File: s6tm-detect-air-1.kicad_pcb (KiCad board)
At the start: 2 copper layers, 67 x 67 mm, 81 parts, among them J1 Conn_01x04, J2 TC2030, J3 Conn_01x04, J4 Conn_01x04, J5 Conn_01x04_Pin, SW1 SW_Push, SW2 SW_Push, U1 SYS1002-H2, U10 004-1-0100, U2 MiCS-5524, U3 LMC6482, U4 HT753-1, U5 SN65HVD230, U6 STM32F103C8Tx, U7 HTU21, U8 LM73100, U9 ENS16x, Y1 8M

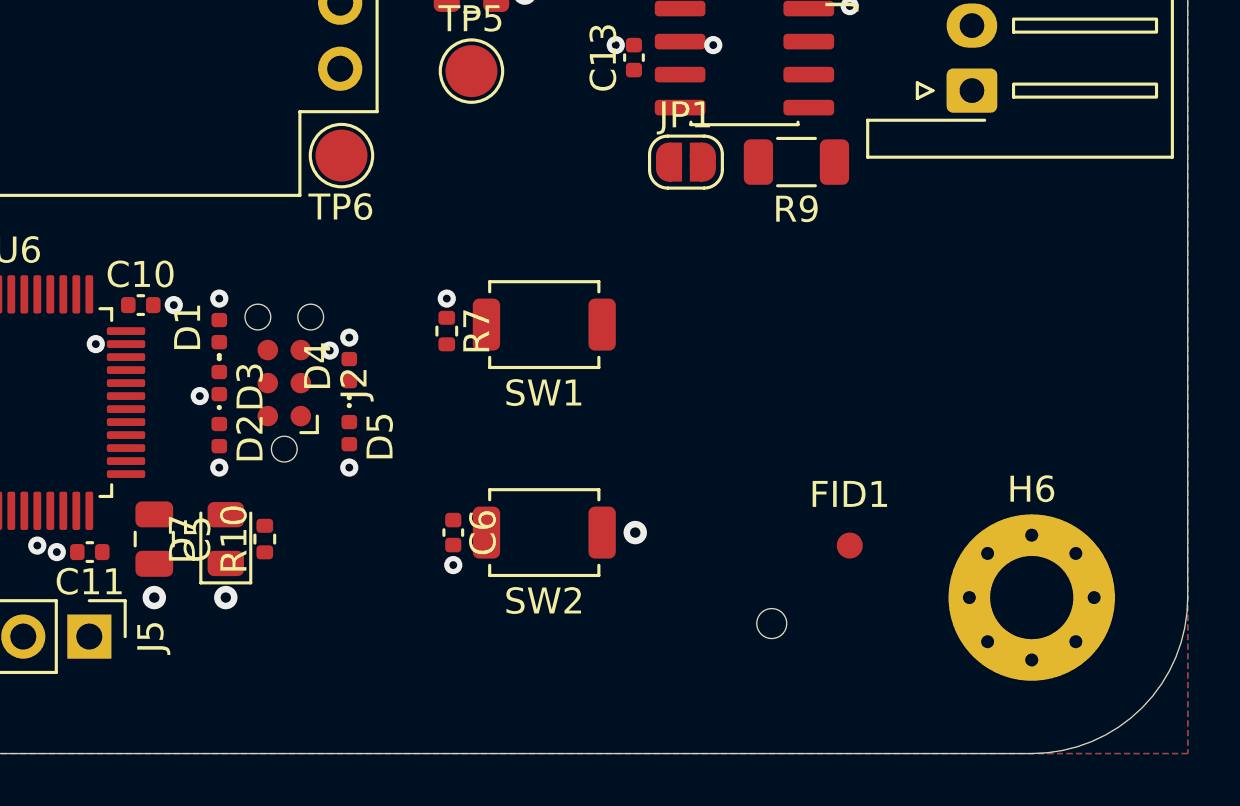
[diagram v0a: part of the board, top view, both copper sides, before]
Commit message: pcb/schem: add spare gpios header
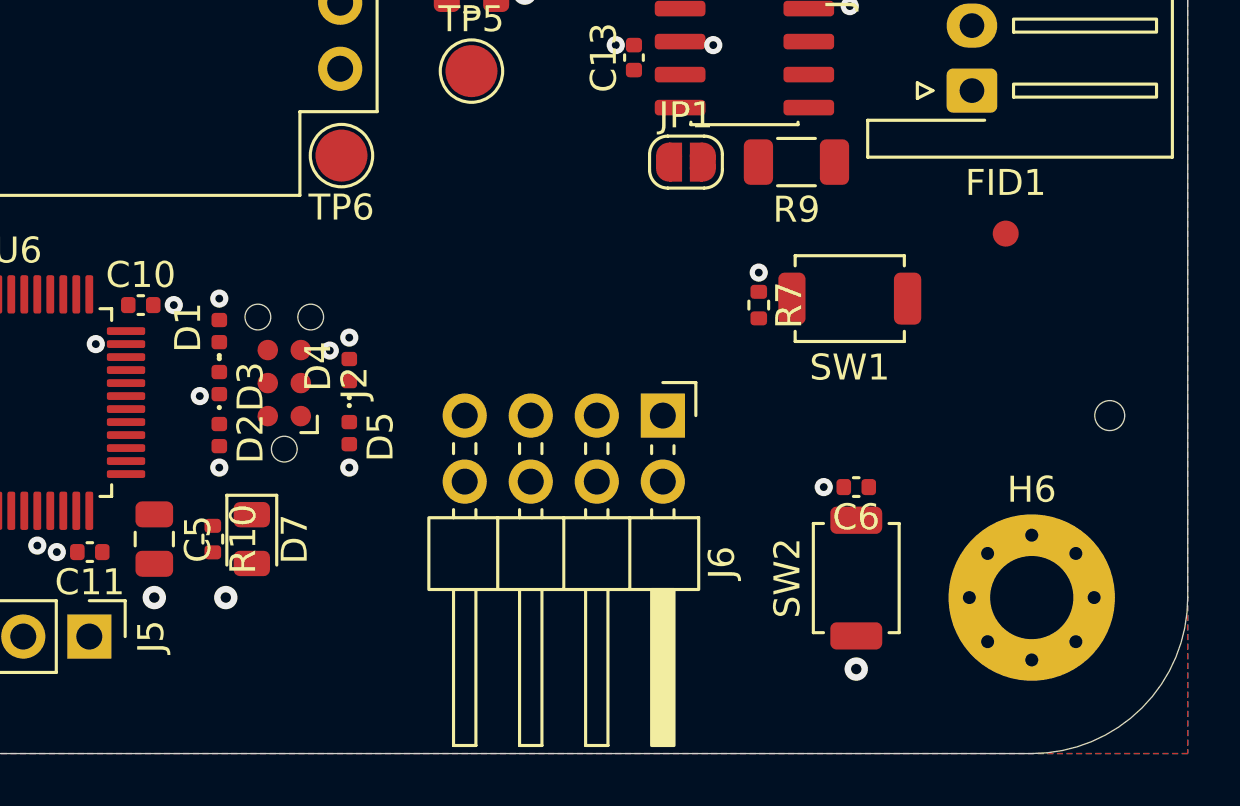
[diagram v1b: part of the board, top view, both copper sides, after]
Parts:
- added J6: Conn_01x08, Connector_PinHeader_2.54mm:PinHeader_2x04_P2.54mm_Horizontal, F.Cu at (161.8, 107.0)
- moved C6 15.6 mm to (169.2, 109.8), turned to 180 degrees
- moved H3 15.3 mm to (179.0, 107.0)
- moved FID1 13.4 mm to (175.0, 100.0)
- moved SW2 12.1 mm to (169.2, 113.2), turned to 90 degrees
- moved R7 12.0 mm to (165.5, 102.8)
- moved SW1 11.8 mm to (169.0, 102.5)
- moved R10 2.00 mm to (144.5, 111.8), turned to -90 degrees
- moved D7 1.00 mm to (146.0, 111.8), turned to -90 degrees
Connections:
- U6 pad 26: unconnected-(U6-PB13-Pad26) -> /PB13
- U6 pad 27: unconnected-(U6-PB14-Pad27) -> /PB14
- U6 pad 28: unconnected-(U6-PB15-Pad28) -> /PB15
- U6 pad 29: unconnected-(U6-PA8-Pad29) -> /PA8

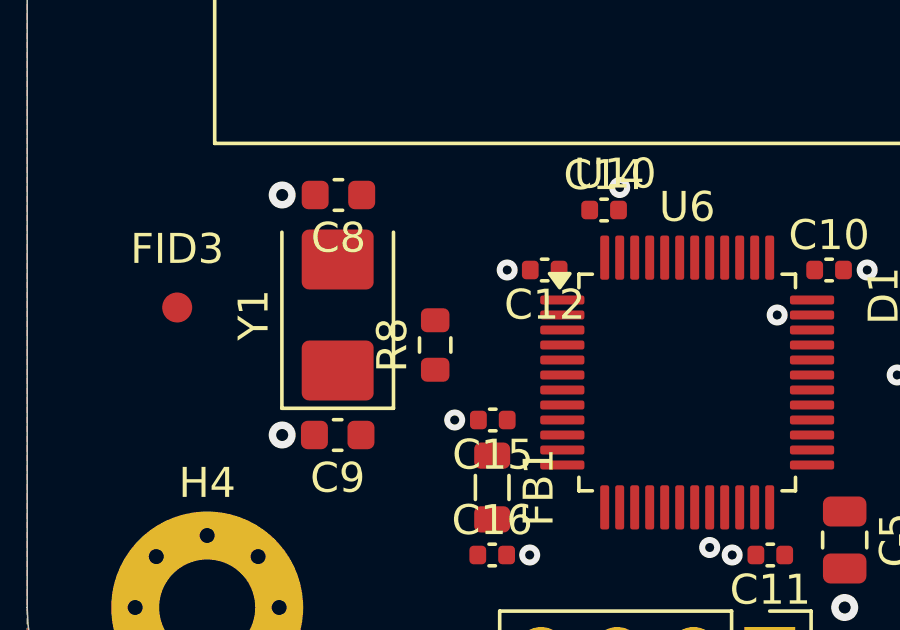
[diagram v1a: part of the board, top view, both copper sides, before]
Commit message: pcb: add crystal routing
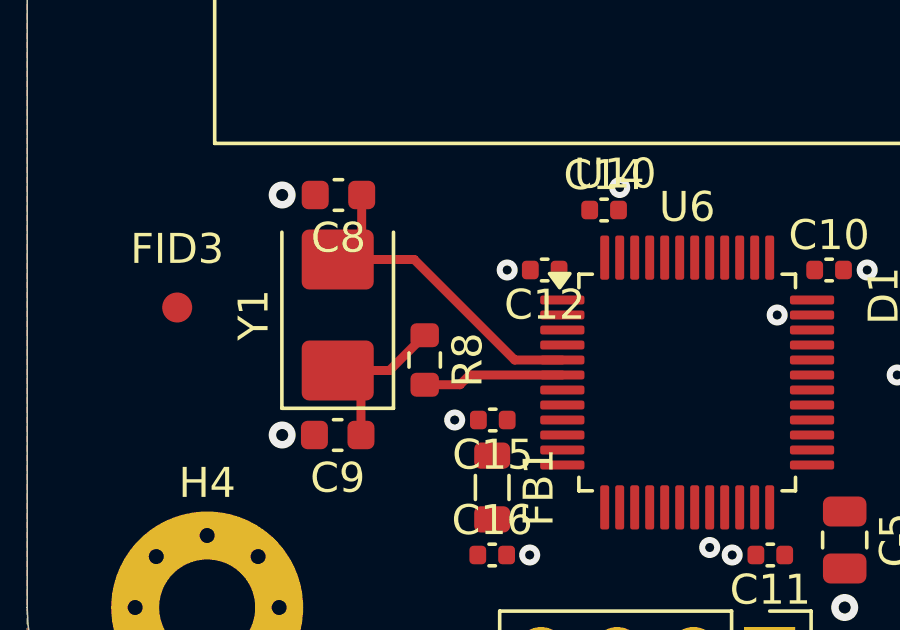
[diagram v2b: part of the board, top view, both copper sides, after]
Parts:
- moved R8 0.61 mm to (128.2, 105.8), turned to -90 degrees
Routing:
- net /XTAL_I: track 0.00 -> 11.4 mm
- net /XTAL_RO: track 0.00 -> 5.86 mm
- net /XTAL_O: track 0.00 -> 4.72 mm
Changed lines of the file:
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@@
 	(footprint "Resistor_SMD:R_0603_1608Metric"
 		(layer "F.Cu")
-		(at 128.6 105.25 90)
+		(at 128.25 105.75 -90)
 		(descr "Resistor SMD 0603 (1608 Metric), square (rectangular) end terminal, IPC-7351 nominal, (Body size source: IPC-SM-782 page 72, https://www.pcb-3d.com/wordpress/wp-content/uploads/ipc-sm-782a_amendment_1_and_2.pdf)")
 		(tags "resistor")
@@
 		)
 		(property "Basic" "Y"
-			(at 0 0 90)
+			(at 0 0 270)
 			(unlocked yes)
 			(layer "F.Fab")
@@
 		)
 		(property "JLCPCB Part #" "C23204"
-			(at 0 0 90)
+			(at 0 0 270)
 			(unlocked yes)
 			(layer "F.Fab")
@@
 		)
 		(property "Manufacturer" "Uniroyal Elec"
-			(at 0 0 90)
+			(at 0 0 270)
 			(unlocked yes)
 			(layer "F.Fab")
@@
 		)
 		(property "Manufacturer Part Number" "0603WAF5600T5E"
-			(at 0 0 90)
+			(at 0 0 270)
 			(unlocked yes)
 			(layer "F.Fab")
@@
 		(duplicate_pad_numbers_are_jumpers no)
 		(fp_line
-			(start -0.237258 -0.5225)
-			(end 0.237258 -0.5225)
+			(start -0.237258 0.5225)
+			(end 0.237258 0.5225)
 			(stroke
 				(width 0.12)
@@
 		)
 		(fp_line
-			(start -0.237258 0.5225)
-			(end 0.237258 0.5225)
+			(start -0.237258 -0.5225)
+			(end 0.237258 -0.5225)
 			(stroke
 				(width 0.12)
@@
 		)
 		(pad "1" smd roundrect
-			(at -0.825 0 90)
+			(at -0.825 0 270)
 			(size 0.8 0.95)
 			(layers "F.Cu" "F.Mask" "F.Paste")
@@
 		)
 		(pad "2" smd roundrect
-			(at 0.825 0 90)
+			(at 0.825 0 270)
 			(size 0.8 0.95)
 			(layers "F.Cu" "F.Mask" "F.Paste")
@@
 		(net "GND")
 	)
+	(segment
+		(start 127.9 102.4)
+		(end 131.25 105.75)
+		(width 0.3)
+		(layer "F.Cu")
+		(net "/XTAL_I")
+	)
+	(segment
+		(start 131.25 105.75)
+		(end 132.8375 105.75)
+		(width 0.3)
+		(layer "F.Cu")
+		(net "/XTAL_I")
+	)
+	(segment
+		(start 125.35 102.4)
+		(end 127.9 102.4)
+		(width 0.3)
+		(layer "F.Cu")
+		(net "/XTAL_I")
+	)
+	(segment
+		(start 126.15 101.6)
+		(end 125.35 102.4)
+		(width 0.3)
+		(layer "F.Cu")
+		(net "/XTAL_I")
+	)
+	(segment
+		(start 126.15 100.25)
+		(end 126.15 101.6)
+		(width 0.3)
+		(layer "F.Cu")
+		(net "/XTAL_I")
+	)
+	(segment
+		(start 128.25 104.925)
+		(end 127.075 106.1)
+		(width 0.3)
+		(layer "F.Cu")
+		(net "/XTAL_RO")
+	)
+	(segment
+		(start 126.125 106.875)
+		(end 125.35 106.1)
+		(width 0.3)
+		(layer "F.Cu")
+		(net "/XTAL_RO")
+	)
+	(segment
+		(start 127.075 106.1)
+		(end 125.35 106.1)
+		(width 0.3)
+		(layer "F.Cu")
+		(net "/XTAL_RO")
+	)
+	(segment
+		(start 126.125 108.25)
+		(end 126.125 106.875)
+		(width 0.3)
+		(layer "F.Cu")
+		(net "/XTAL_RO")
+	)
+	(segment
+		(start 129.75 106.25)
+		(end 129.425 106.575)
+		(width 0.3)
+		(layer "F.Cu")
+		(net "/XTAL_O")
+	)
+	(segment
+		(start 132.8375 106.25)
+		(end 129.75 106.25)
+		(width 0.3)
+		(layer "F.Cu")
+		(net "/XTAL_O")
+	)
+	(segment
+		(start 129.425 106.575)
+		(end 128.25 106.575)
+		(width 0.3)
+		(layer "F.Cu")
+		(net "/XTAL_O")
+	)
 	(zone

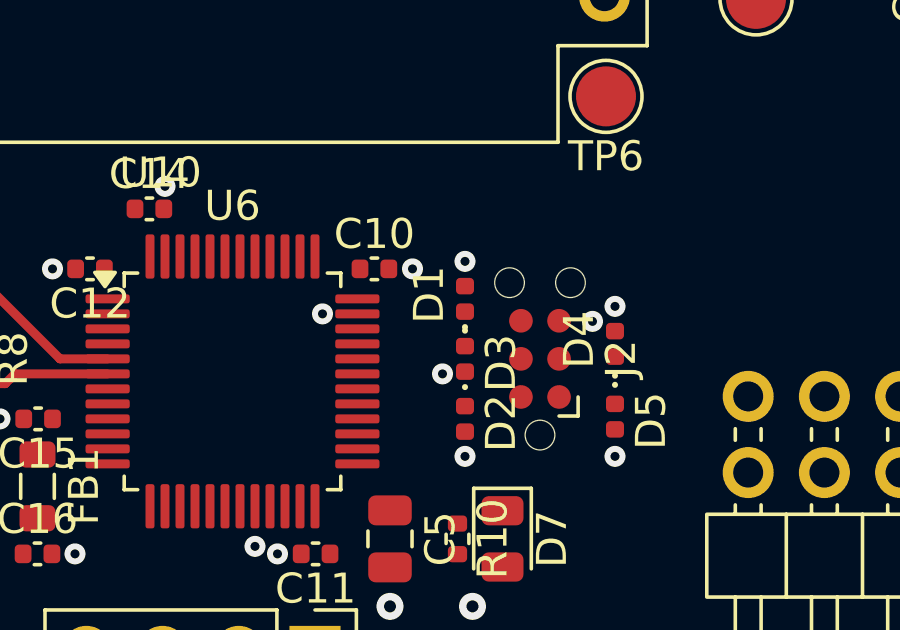
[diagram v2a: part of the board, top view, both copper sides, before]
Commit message: pcb: add swd routing
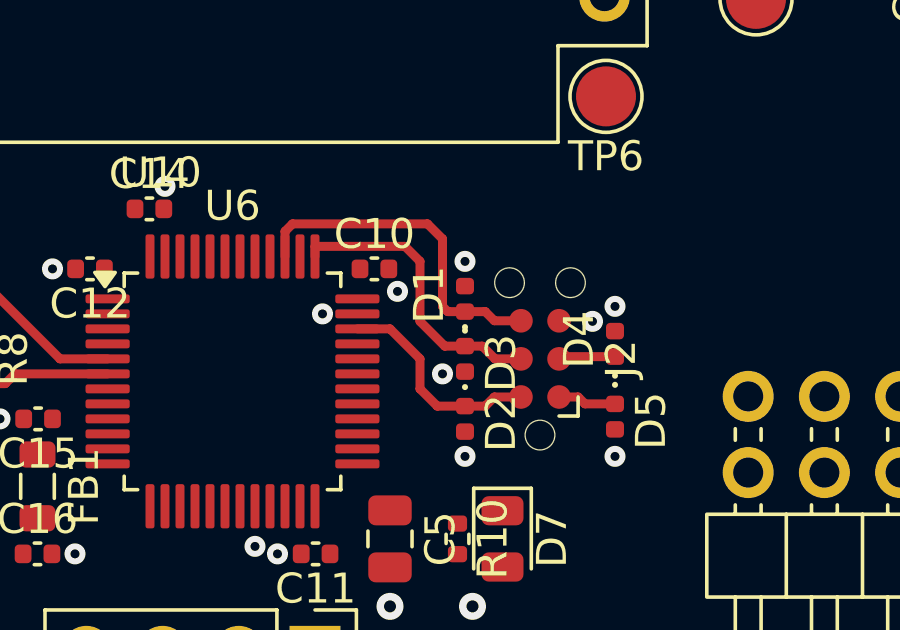
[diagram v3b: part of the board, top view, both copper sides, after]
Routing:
- net /SWO: track 0.00 -> 11.5 mm
- net /SWCLK: track 0.00 -> 9.93 mm
- net /SWDIO: track 0.00 -> 7.23 mm
- net +3V3: track 0.00 -> 1.96 mm
- net /NRST: track 0.00 -> 1.90 mm
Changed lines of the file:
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@@
 	)
 	(via
-		(at 143 102.75)
+		(at 142.5 103.5)
 		(size 0.7)
 		(drill 0.3)
@@
 		(free yes)
 		(net "GND")
+	)
+	(segment
+		(start 149.75 107.25)
+		(end 148.75 107.25)
+		(width 0.3)
+		(layer "F.Cu")
+		(net "+3V3")
+	)
+	(segment
+		(start 148.75 107.25)
+		(end 148.52 107.02)
+		(width 0.3)
+		(layer "F.Cu")
+		(net "+3V3")
+	)
+	(segment
+		(start 147.885 107.02)
+		(end 148.52 107.02)
+		(width 0.3)
+		(layer "F.Cu")
+		(net "+3V3")
 	)
 	(segment
@@
 	)
 	(segment
+		(start 139 101.25)
+		(end 138.75 101.5)
+		(width 0.3)
+		(layer "F.Cu")
+		(net "/SWO")
+	)
+	(segment
+		(start 144.75 104.175)
+		(end 144.175 104.175)
+		(width 0.3)
+		(layer "F.Cu")
+		(net "/SWO")
+	)
+	(segment
+		(start 144 101.75)
+		(end 143.5 101.25)
+		(width 0.3)
+		(layer "F.Cu")
+		(net "/SWO")
+	)
+	(segment
+		(start 143.5 101.25)
+		(end 139 101.25)
+		(width 0.3)
+		(layer "F.Cu")
+		(net "/SWO")
+	)
+	(segment
+		(start 144 104)
+		(end 144 101.75)
+		(width 0.3)
+		(layer "F.Cu")
+		(net "/SWO")
+	)
+	(segment
+		(start 144.75 104.175)
+		(end 145.425 104.175)
+		(width 0.3)
+		(layer "F.Cu")
+		(net "/SWO")
+	)
+	(segment
+		(start 145.73 104.48)
+		(end 146.615 104.48)
+		(width 0.3)
+		(layer "F.Cu")
+		(net "/SWO")
+	)
+	(segment
+		(start 144.175 104.175)
+		(end 144 104)
+		(width 0.3)
+		(layer "F.Cu")
+		(net "/SWO")
+	)
+	(segment
+		(start 138.75 101.5)
+		(end 138.75 102.3375)
+		(width 0.3)
+		(layer "F.Cu")
+		(net "/SWO")
+	)
+	(segment
+		(start 145.425 104.175)
+		(end 145.73 104.48)
+		(width 0.3)
+		(layer "F.Cu")
+		(net "/SWO")
+	)
+	(segment
 		(start 129.75 106.25)
 		(end 129.425 106.575)
@@
 		(net "/XTAL_O")
 	)
+	(segment
+		(start 149.75 105.675)
+		(end 147.96 105.675)
+		(width 0.3)
+		(layer "F.Cu")
+		(net "/NRST")
+	)
+	(segment
+		(start 147.96 105.675)
+		(end 147.885 105.75)
+		(width 0.3)
+		(layer "F.Cu")
+		(net "/NRST")
+	)
+	(segment
+		(start 143.25 105.75)
+		(end 142.25 104.75)
+		(width 0.3)
+		(layer "F.Cu")
+		(net "/SWDIO")
+	)
+	(segment
+		(start 143.825 107.325)
+		(end 143.25 106.75)
+		(width 0.3)
+		(layer "F.Cu")
+		(net "/SWDIO")
+	)
+	(segment
+		(start 142.25 104.75)
+		(end 141.1625 104.75)
+		(width 0.3)
+		(layer "F.Cu")
+		(net "/SWDIO")
+	)
+	(segment
+		(start 143.25 106.75)
+		(end 143.25 105.75)
+		(width 0.3)
+		(layer "F.Cu")
+		(net "/SWDIO")
+	)
+	(segment
+		(start 145.73 107.02)
+		(end 146.615 107.02)
+		(width 0.3)
+		(layer "F.Cu")
+		(net "/SWDIO")
+	)
+	(segment
+		(start 144.75 107.325)
+		(end 143.825 107.325)
+		(width 0.3)
+		(layer "F.Cu")
+		(net "/SWDIO")
+	)
+	(segment
+		(start 144.75 107.325)
+		(end 145.425 107.325)
+		(width 0.3)
+		(layer "F.Cu")
+		(net "/SWDIO")
+	)
+	(segment
+		(start 145.425 107.325)
+		(end 145.73 107.02)
+		(width 0.3)
+		(layer "F.Cu")
+		(net "/SWDIO")
+	)
+	(segment
+		(start 145.325 105.325)
+		(end 145.75 105.75)
+		(width 0.3)
+		(layer "F.Cu")
+		(net "/SWCLK")
+	)
+	(segment
+		(start 144.075 105.325)
+		(end 143.25 104.5)
+		(width 0.3)
+		(layer "F.Cu")
+		(net "/SWCLK")
+	)
+	(segment
+		(start 139.75 102)
+		(end 139.75 102.3375)
+		(width 0.3)
+		(layer "F.Cu")
+		(net "/SWCLK")
+	)
+	(segment
+		(start 144.75 105.325)
+		(end 144.075 105.325)
+		(width 0.3)
+		(layer "F.Cu")
+		(net "/SWCLK")
+	)
+	(segment
+		(start 144.75 105.325)
+		(end 145.325 105.325)
+		(width 0.3)
+		(layer "F.Cu")
+		(net "/SWCLK")
+	)
+	(segment
+		(start 145.75 105.75)
+		(end 146.615 105.75)
+		(width 0.3)
+		(layer "F.Cu")
+		(net "/SWCLK")
+	)
+	(segment
+		(start 143.25 102.5)
+		(end 142.75 102)
+		(width 0.3)
+		(layer "F.Cu")
+		(net "/SWCLK")
+	)
+	(segment
+		(start 142.75 102)
+		(end 139.75 102)
+		(width 0.3)
+		(layer "F.Cu")
+		(net "/SWCLK")
+	)
+	(segment
+		(start 143.25 104.5)
+		(end 143.25 102.5)
+		(width 0.3)
+		(layer "F.Cu")
+		(net "/SWCLK")
+	)
 	(zone

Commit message: pcb: add can routing
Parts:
- moved C14 0.23 mm to (134.0, 100.8)
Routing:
- net /CAN_TX: track 0.00 -> 36.4 mm
- net /CAN_RX: track 0.00 -> 31.9 mm
- net /CANL: track 0.00 -> 17.2 mm
- net /CANH: track 0.00 -> 14.8 mm
- net Net-(JP1-B): track 0.00 -> 2.14 mm
- net +3V3: track 1.96 -> 3.81 mm
